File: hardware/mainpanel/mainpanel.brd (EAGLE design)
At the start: 80 x 80 mm, 25 parts, among them J1 CDH, J2 OW, J3 DBG, J4 SUN-UART, J5 ADCS, J6 ENV, J7 SUN, U1 DS18B20, U2 DS18B20, U3 DS18B20

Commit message: Move components
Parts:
- moved U2 3.76 mm to (40.8, 55.0), turned to 90 degrees
- moved R1 3.61 mm to (35.0, 56.0)
- moved C2 3.16 mm to (29.5, 56.0)
- moved C7 2.00 mm to (7.00, 50.0)
- moved J4 2.00 mm to (10.0, 41.0)
- moved J7 2.00 mm to (16.0, 55.0)
- moved U3 1.41 mm to (31.0, 74.0), turned to 180 degrees
- moved C5 1.00 mm to (7.00, 60.0)
- moved J2 1.00 mm to (34.0, 63.0)
- moved J3 1.00 mm to (49.0, 63.0)
- moved J5 1.00 mm to (16.0, 65.0)
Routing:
- net VCC: track 0.00 -> 8.28 mm, vias 0 -> 1

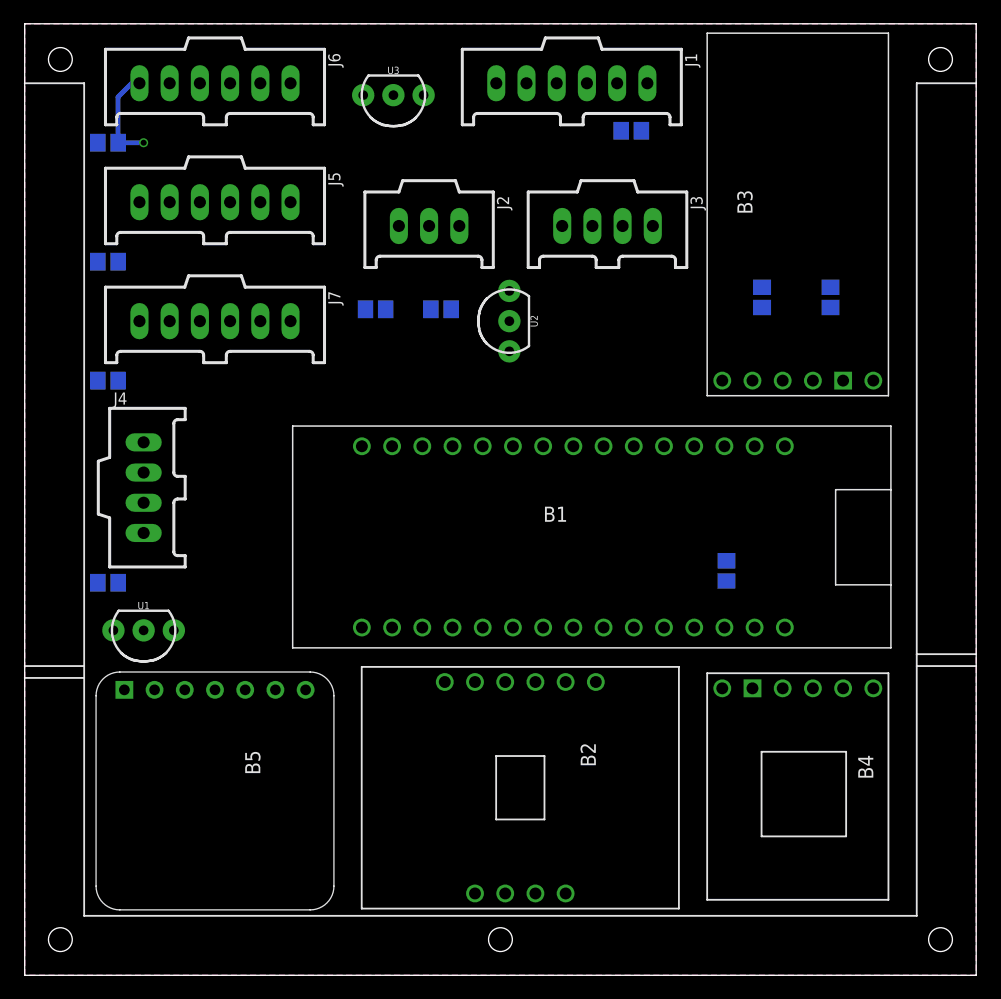
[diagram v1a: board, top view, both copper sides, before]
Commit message: Add power connections
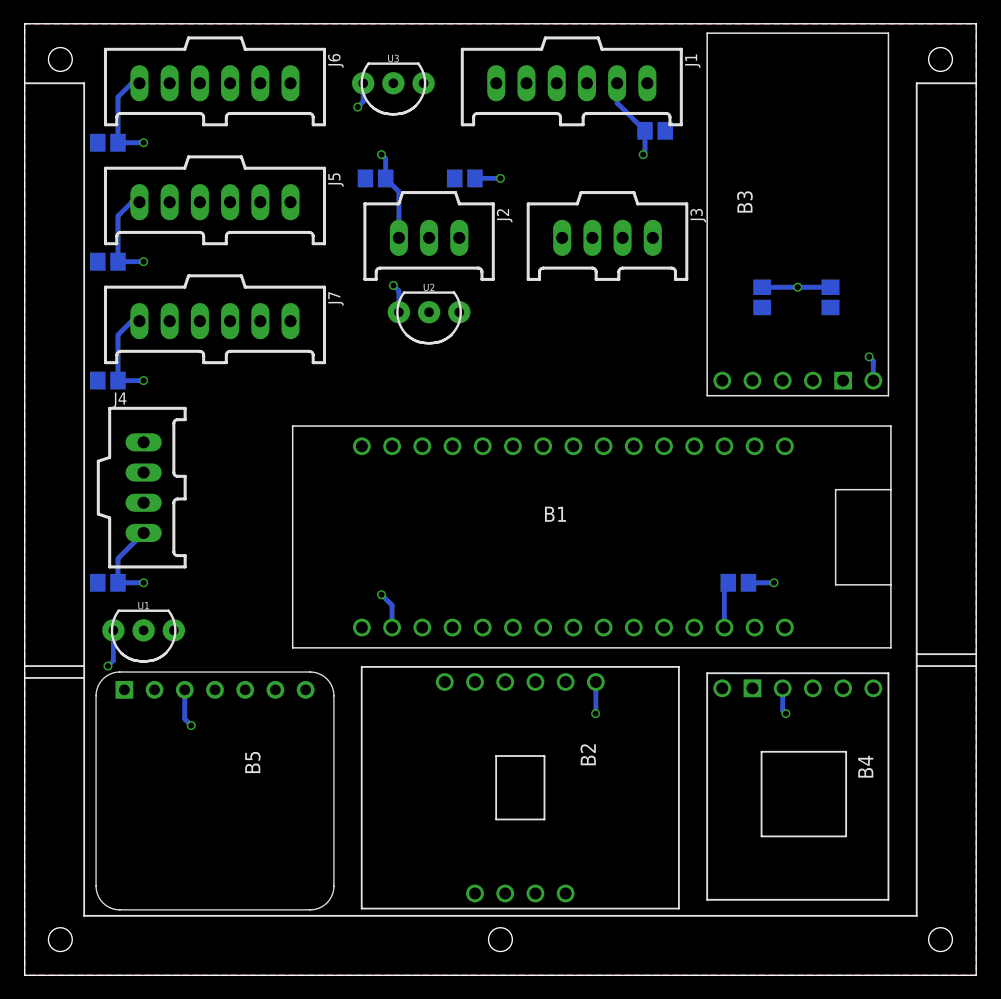
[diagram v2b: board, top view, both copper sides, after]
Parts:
- moved R1 11.2 mm to (37.0, 67.0)
- moved C2 11.0 mm to (29.5, 67.0)
- moved U2 6.79 mm to (34.0, 55.8), turned to 180 degrees
- moved C1 2.00 mm to (53.0, 71.0)
- moved R2 1.41 mm to (60.0, 33.0), turned to 0 degrees
- moved J2 1.00 mm to (34.0, 62.0)
- moved J3 1.00 mm to (49.0, 62.0)
- moved U3 1.00 mm to (31.0, 75.0)
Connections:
- net TEMP-OW: now also R1.1; no longer R1.2
- net VCC: now also R1.2; no longer R1.1
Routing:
- net VCC: track 8.28 -> 78.0 mm, vias 1 -> 17
- net NUC-RST: track 0.00 -> 3.89 mm

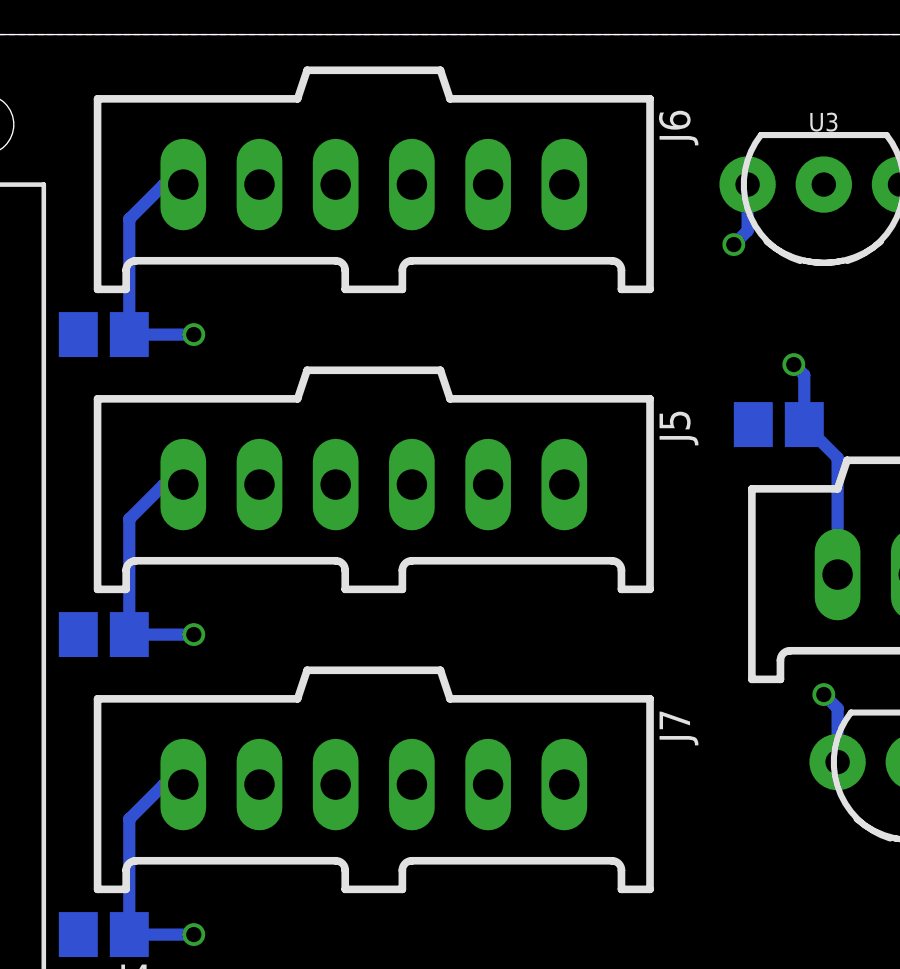
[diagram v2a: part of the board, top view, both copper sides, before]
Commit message: Update spi connectors
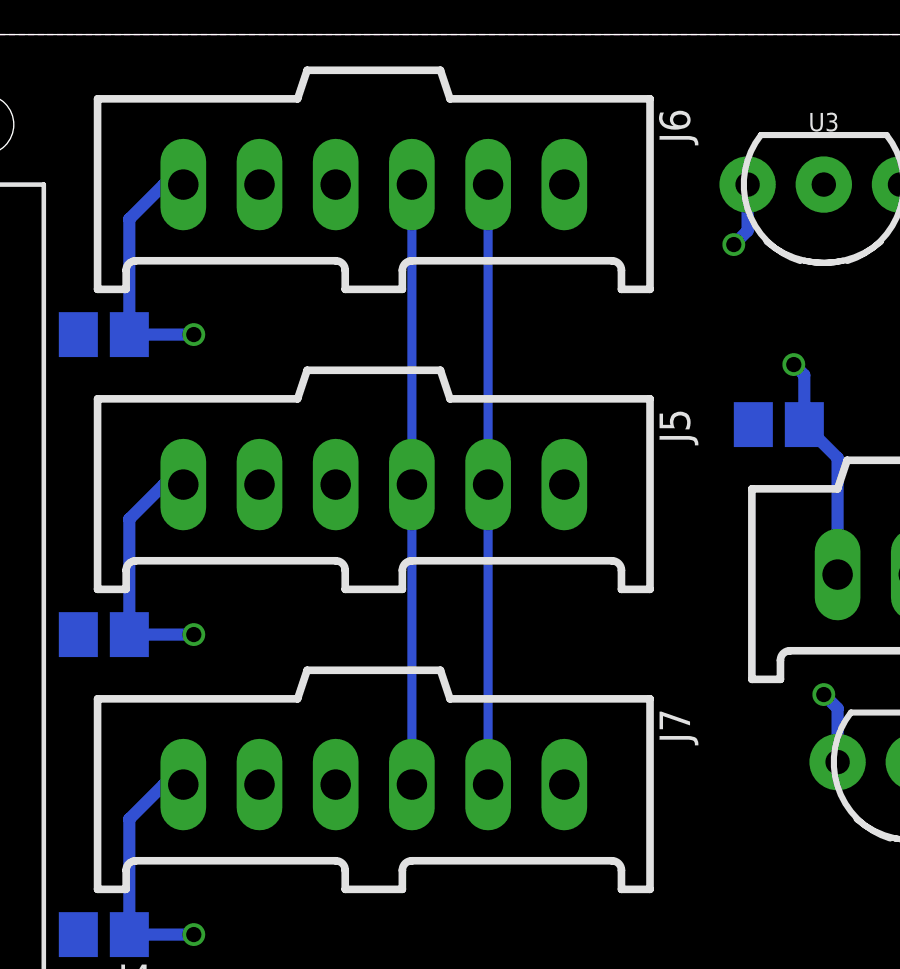
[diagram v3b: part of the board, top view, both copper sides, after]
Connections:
- net GND: now also J5.5, J6.5, J7.5; no longer J5.4, J6.4, J7.4
- net SPI-SCK: now also J5.4, J6.4, J7.4; no longer J5.5, J6.5, J7.5
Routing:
- net SPI-MOSI: track 0.00 -> 20.0 mm
- net SPI-MISO: track 0.00 -> 20.0 mm
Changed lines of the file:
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@@
 <contactref element="C4" pad="1"/>
 <contactref element="B5" pad="GND"/>
-<contactref element="J7" pad="4"/>
-<contactref element="J6" pad="4"/>
-<contactref element="J5" pad="4"/>
-<contactref element="C7" pad="1"/>
+<contactref element="J5" pad="5"/>
+<contactref element="J6" pad="5"/>
+<contactref element="J7" pad="5"/>
 <contactref element="C6" pad="1"/>
 <contactref element="C5" pad="1"/>
+<contactref element="C7" pad="1"/>
+<wire x1="53.85" y1="71" x2="52.35" y2="75" width="0" layer="19" extent="16-16"/>
+<wire x1="42.19" y1="75" x2="52.35" y2="75" width="0" layer="19" extent="1-1"/>
+<wire x1="33.54" y1="75" x2="42.19" y2="75" width="0" layer="19" extent="1-1"/>
+<wire x1="28.65" y1="67" x2="33.54" y2="75" width="0" layer="19" extent="16-16"/>
+<wire x1="36.54" y1="62" x2="28.65" y2="67" width="0" layer="19" extent="16-16"/>
+<wire x1="36.54" y1="55.75" x2="36.54" y2="62" width="0" layer="19" extent="1-1"/>
+<wire x1="12.19" y1="65" x2="28.65" y2="67" width="0" layer="19" extent="16-16"/>
+<wire x1="6.15" y1="70" x2="12.19" y2="65" width="0" layer="19" extent="16-16"/>
+<wire x1="12.19" y1="75" x2="6.15" y2="70" width="0" layer="19" extent="16-16"/>
+<wire x1="6.15" y1="60" x2="12.19" y2="65" width="0" layer="19" extent="16-16"/>
+<wire x1="12.19" y1="55" x2="6.15" y2="60" width="0" layer="19" extent="16-16"/>
+<wire x1="6.15" y1="50" x2="12.19" y2="55" width="0" layer="19" extent="16-16"/>
+<wire x1="10" y1="44.81" x2="6.15" y2="50" width="0" layer="19" extent="16-16"/>
+<wire x1="6.15" y1="33" x2="10" y2="44.81" width="0" layer="19" extent="16-16"/>
+<wire x1="12.54" y1="29" x2="6.15" y2="33" width="0" layer="19" extent="16-16"/>
+<wire x1="8.38" y1="24" x2="12.54" y2="29" width="0" layer="19" extent="1-1"/>
+<wire x1="56.29" y1="44.48" x2="36.54" y2="55.75" width="0" layer="19" extent="1-1"/>
+<wire x1="68.81" y1="50" x2="56.29" y2="44.48" width="0" layer="19" extent="1-1"/>
+<wire x1="61.37" y1="29.24" x2="56.29" y2="44.48" width="0" layer="19" extent="1-1"/>
+<wire x1="61.19" y1="24.128" x2="61.37" y2="29.24" width="0" layer="19" extent="1-1"/>
+<wire x1="42.94" y1="24.66" x2="61.19" y2="24.128" width="0" layer="19" extent="1-1"/>
 </signal>
 <signal name="IMU-SDA">
@@
 <contactref element="J6" pad="3"/>
 <contactref element="J5" pad="3"/>
+<wire x1="17.27" y1="75" x2="17.27" y2="65" width="0.3048" layer="16"/>
+<wire x1="17.27" y1="65" x2="17.27" y2="55" width="0.3048" layer="16"/>
 <wire x1="17.27" y1="55" x2="53.75" y2="44.48" width="0" layer="19" extent="1-1"/>
-<wire x1="17.27" y1="65" x2="17.27" y2="55" width="0" layer="19" extent="1-1"/>
-<wire x1="17.27" y1="75" x2="17.27" y2="65" width="0" layer="19" extent="1-1"/>
 <wire x1="18.54" y1="24" x2="17.27" y2="55" width="0" layer="19" extent="1-1"/>
 </signal>
@@
 <contactref element="B1" pad="A1"/>
 <contactref element="B5" pad="SCL/SCK"/>
-<contactref element="J5" pad="5"/>
-<contactref element="J6" pad="5"/>
-<contactref element="J7" pad="5"/>
-<wire x1="12.19" y1="65" x2="12.19" y2="75" width="0" layer="19" extent="1-1"/>
-<wire x1="12.19" y1="55" x2="12.19" y2="65" width="0" layer="19" extent="1-1"/>
-<wire x1="16" y1="24" x2="12.19" y2="55" width="0" layer="19" extent="1-1"/>
+<contactref element="J5" pad="4"/>
+<contactref element="J6" pad="4"/>
+<contactref element="J7" pad="4"/>
+<wire x1="14.73" y1="65" x2="14.73" y2="75" width="0" layer="19" extent="1-1"/>
+<wire x1="14.73" y1="55" x2="14.73" y2="65" width="0" layer="19" extent="1-1"/>
+<wire x1="16" y1="24" x2="14.73" y2="55" width="0" layer="19" extent="1-1"/>
 <wire x1="38.51" y1="29.24" x2="16" y2="24" width="0" layer="19" extent="1-1"/>
 </signal>
@@
 <contactref element="J6" pad="2"/>
 <contactref element="J5" pad="2"/>
-<wire x1="19.81" y1="65" x2="19.81" y2="75" width="0" layer="19" extent="1-1"/>
-<wire x1="19.81" y1="55" x2="19.81" y2="65" width="0" layer="19" extent="1-1"/>
-<wire x1="21.08" y1="24" x2="19.81" y2="55" width="0" layer="19" extent="1-1"/>
-<wire x1="48.67" y1="29.24" x2="21.08" y2="24" width="0" layer="19" extent="1-1"/>
+<wire x1="19.81" y1="75" x2="19.81" y2="65" width="0.3048" layer="16"/>
+<wire x1="19.81" y1="65" x2="19.81" y2="55" width="0.3048" layer="16"/>
+<wire x1="21.08" y1="24" x2="48.67" y2="29.24" width="0" layer="19" extent="1-1"/>
+<wire x1="19.81" y1="55" x2="21.08" y2="24" width="0" layer="19" extent="1-1"/>
 </signal>
 <signal name="SPI-CS-ENV">

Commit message: Route board
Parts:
- moved R5 2.83 mm to (65.8, 59.0)
- moved R6 2.83 mm to (60.0, 59.0)
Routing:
- net SPI-SCK: track 0.00 -> 84.8 mm, vias 0 -> 2
- net TEMP-OW: track 0.00 -> 76.0 mm, vias 0 -> 4
- net SPI-MISO: track 20.0 -> 90.6 mm, vias 0 -> 2
- net SPI-MOSI: track 20.0 -> 90.5 mm, vias 0 -> 2
- net SPI-CS-ENV: track 0.00 -> 53.0 mm, vias 0 -> 2
- net GPS-SCL: track 0.00 -> 45.0 mm
- net SUN-RX: track 0.00 -> 41.0 mm, vias 0 -> 2
- net CDH-TX: track 0.00 -> 40.6 mm
- net CDH-RX: track 0.00 -> 40.3 mm
- net IMU-SDA: track 0.00 -> 40.1 mm
- net GPS-SDA: track 0.00 -> 39.3 mm
- net DBG-RX: track 0.00 -> 37.7 mm
- net SPI-CS-ADCS: track 0.00 -> 37.5 mm, vias 0 -> 2
- net DBG-TX: track 0.00 -> 36.6 mm
- net SUN-TX: track 0.00 -> 33.1 mm, vias 0 -> 2
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
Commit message: Improve layout
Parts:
- moved R5 4.14 mm to (62.0, 57.2), turned to 0 degrees
- moved C1 3.16 mm to (50.0, 70.0), turned to 90 degrees
- moved J3 3.16 mm to (48.0, 59.0)
- moved R1 3.16 mm to (34.0, 68.0), turned to 0 degrees
- moved R6 2.00 mm to (60.0, 61.0), turned to 0 degrees
- moved U3 1.41 mm to (32.0, 76.0)
- moved C2 1.00 mm to (29.5, 68.0), turned to 0 degrees
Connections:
- net GND: now also C2.2; no longer C2.1
- net VCC: now also C2.1; no longer C2.2
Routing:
- net VCC: track 69.1 -> 74.4 mm, vias 15 -> 17
- net TEMP-OW: track 76.0 -> 71.8 mm, vias 4 -> 2
- net DBG-TX: track 36.6 -> 33.2 mm
- net DBG-RX: track 37.7 -> 34.3 mm
- net GPS-SCL: track 45.0 -> 41.9 mm
- net GPS-TX: track 24.0 -> 21.4 mm
- net GPS-RX: track 24.0 -> 21.4 mm
- net GPS-SDA: track 39.3 -> 41.8 mm
- net CDH-RX: track 40.3 -> 42.6 mm
- net SPI-MOSI: track 90.5 -> 89.2 mm
- net CDH-TX: track 40.6 -> 41.7 mm
- net SPI-MISO: track 90.6 -> 89.7 mm
- net SUN-TX: track 33.1 -> 32.6 mm
